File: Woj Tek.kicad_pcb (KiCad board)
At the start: 2 copper layers, 73.6 x 46.2 mm, 31 parts, among them J1 AVR-ISP-6, J2 Conn_01x02, J3 Conn_01x02, J4 Conn_01x02, Q1 BC547, Q2 BC547, Q3 AO3400A, Q4 BC547, SW1 SW_Push, SW2 SW_Push, U1 L7805, U2 ATtiny85-20P

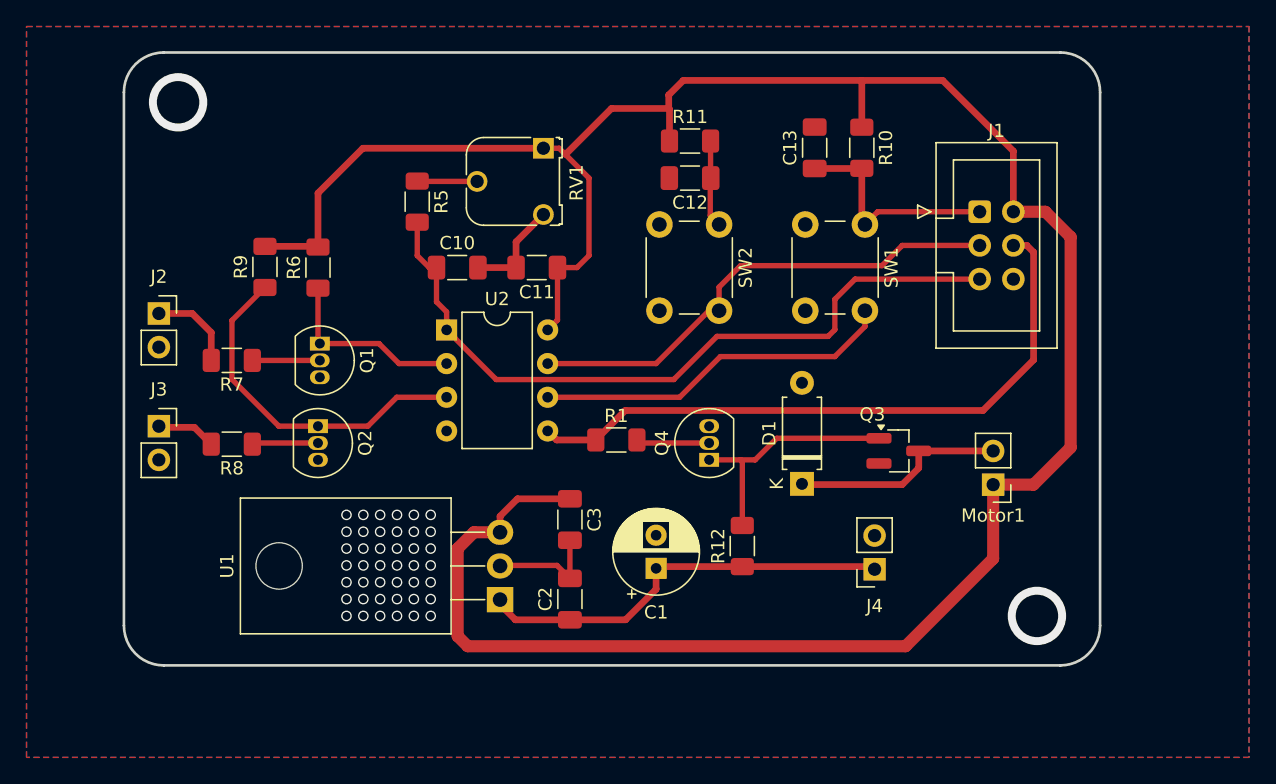
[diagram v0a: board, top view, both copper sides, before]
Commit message: Correction in designators.
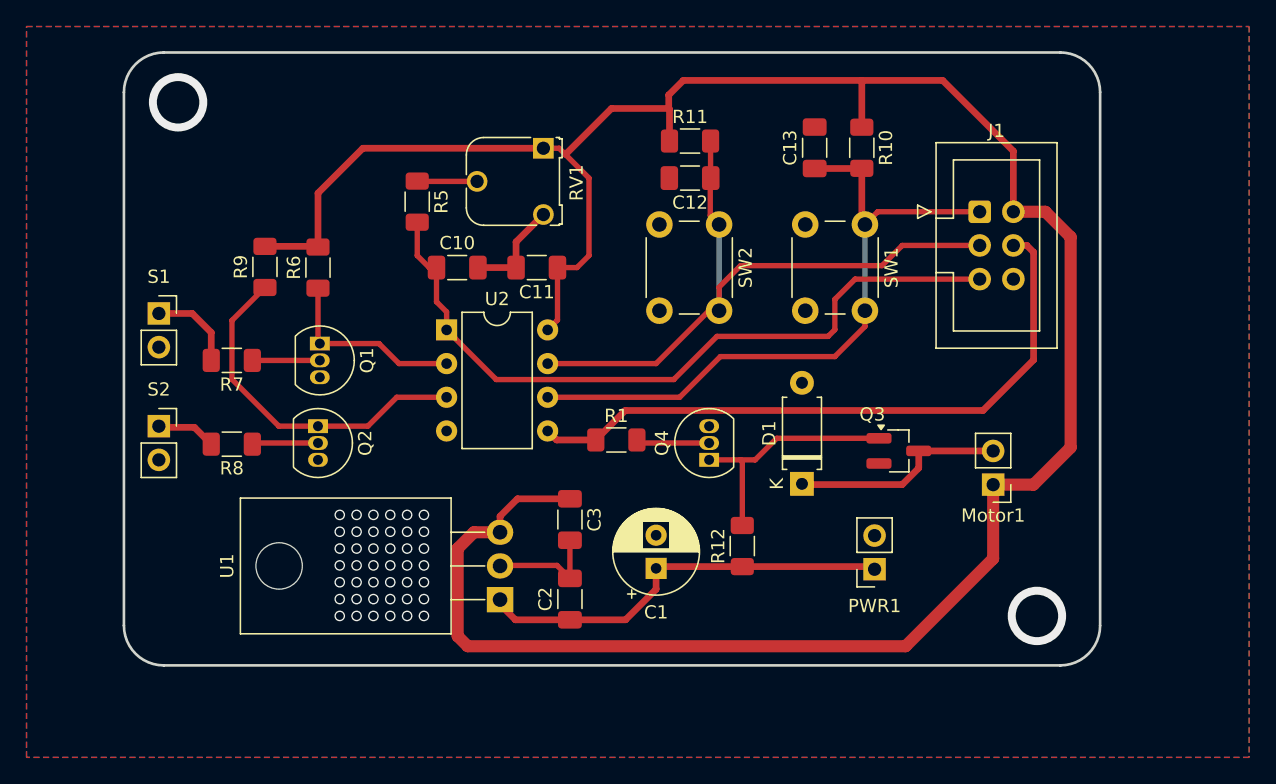
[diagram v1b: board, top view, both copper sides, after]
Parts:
- renumbered J4 to PWR1, J2 to S1, J3 to S2
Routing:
- net /MCU/PB2: track 43.9 -> 50.4 mm
- net /MCU/PB1: track 44.3 -> 50.8 mm
